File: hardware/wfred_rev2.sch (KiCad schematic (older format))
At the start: 8 parts, among them U101 L6920D

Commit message: Changed schematic to AA batteries and holder
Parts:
- removed B101: BATT_HOLDER, myFootprints:KEYSTONE1013, symbol BATT_HOLDER
- added B?: BATT_HOLDER_2, symbol BATT_HOLDER_2
- C101, C102, C104, C105: value 22u/25V -> 22u
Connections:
- wire segments 26 -> 25
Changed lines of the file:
@@
 P 2150 2900
 F 0 "C101" H 2150 3000 40  0000 L CNN
-F 1 "22u/25V" H 2156 2815 40  0000 L CNN
+F 1 "22u" H 2156 2815 40  0000 L CNN
 F 2 "Capacitors_SMD:C_0805_HandSoldering" H 2188 2750 30  0001 C CNN
 F 3 "" H 2150 2900 60  0000 C CNN
@@
 P 2450 2900
 F 0 "C102" H 2450 3000 40  0000 L CNN
-F 1 "22u/25V" H 2456 2815 40  0000 L CNN
+F 1 "22u" H 2456 2815 40  0000 L CNN
 F 2 "Capacitors_SMD:C_0805_HandSoldering" H 2488 2750 30  0001 C CNN
 F 3 "" H 2450 2900 60  0000 C CNN
@@
 P 6300 2600
 F 0 "C104" H 6300 2700 40  0000 L CNN
-F 1 "22u/25V" H 6306 2515 40  0000 L CNN
+F 1 "22u" H 6306 2515 40  0000 L CNN
 F 2 "Capacitors_SMD:C_0805_HandSoldering" H 6338 2450 30  0001 C CNN
 F 3 "" H 6300 2600 60  0000 C CNN
@@
 P 6600 2600
 F 0 "C105" H 6600 2700 40  0000 L CNN
-F 1 "22u/25V" H 6606 2515 40  0000 L CNN
+F 1 "22u" H 6606 2515 40  0000 L CNN
 F 2 "Capacitors_SMD:C_0805_HandSoldering" H 6638 2450 30  0001 C CNN
 F 3 "" H 6600 2600 60  0000 C CNN
@@
 $EndSheet
 Wire Wire Line
-	900  6100 1500 6100
-Wire Wire Line
 	900  3700 900  2600
 Wire Wire Line
 	1500 3700 1500 2800
 $Comp
-L BATT_HOLDER B101
-U 1 1 5A14A6C1
+L BATT_HOLDER_2 B?
+U 1 1 5BE48F43
 P 1200 4900
-F 0 "B101" H 1200 5000 60  0000 C CNN
-F 1 "BATT_HOLDER" H 1200 4900 60  0000 C CNN
-F 2 "myFootprints:KEYSTONE1013" H 1200 4900 60  0001 C CNN
+F 0 "B?" H 1200 5000 60  0000 C CNN
+F 1 "BATT_HOLDER_2" H 1200 4900 60  0000 C CNN
+F 2 "" H 1200 4900 60  0001 C CNN
 F 3 "" H 1200 4900 60  0001 C CNN
-F 4 "KEYSTONE 1013" H 1200 4900 60  0001 C CNN "Reichelt"
 	1    1200 4900
 	0    1    1    0

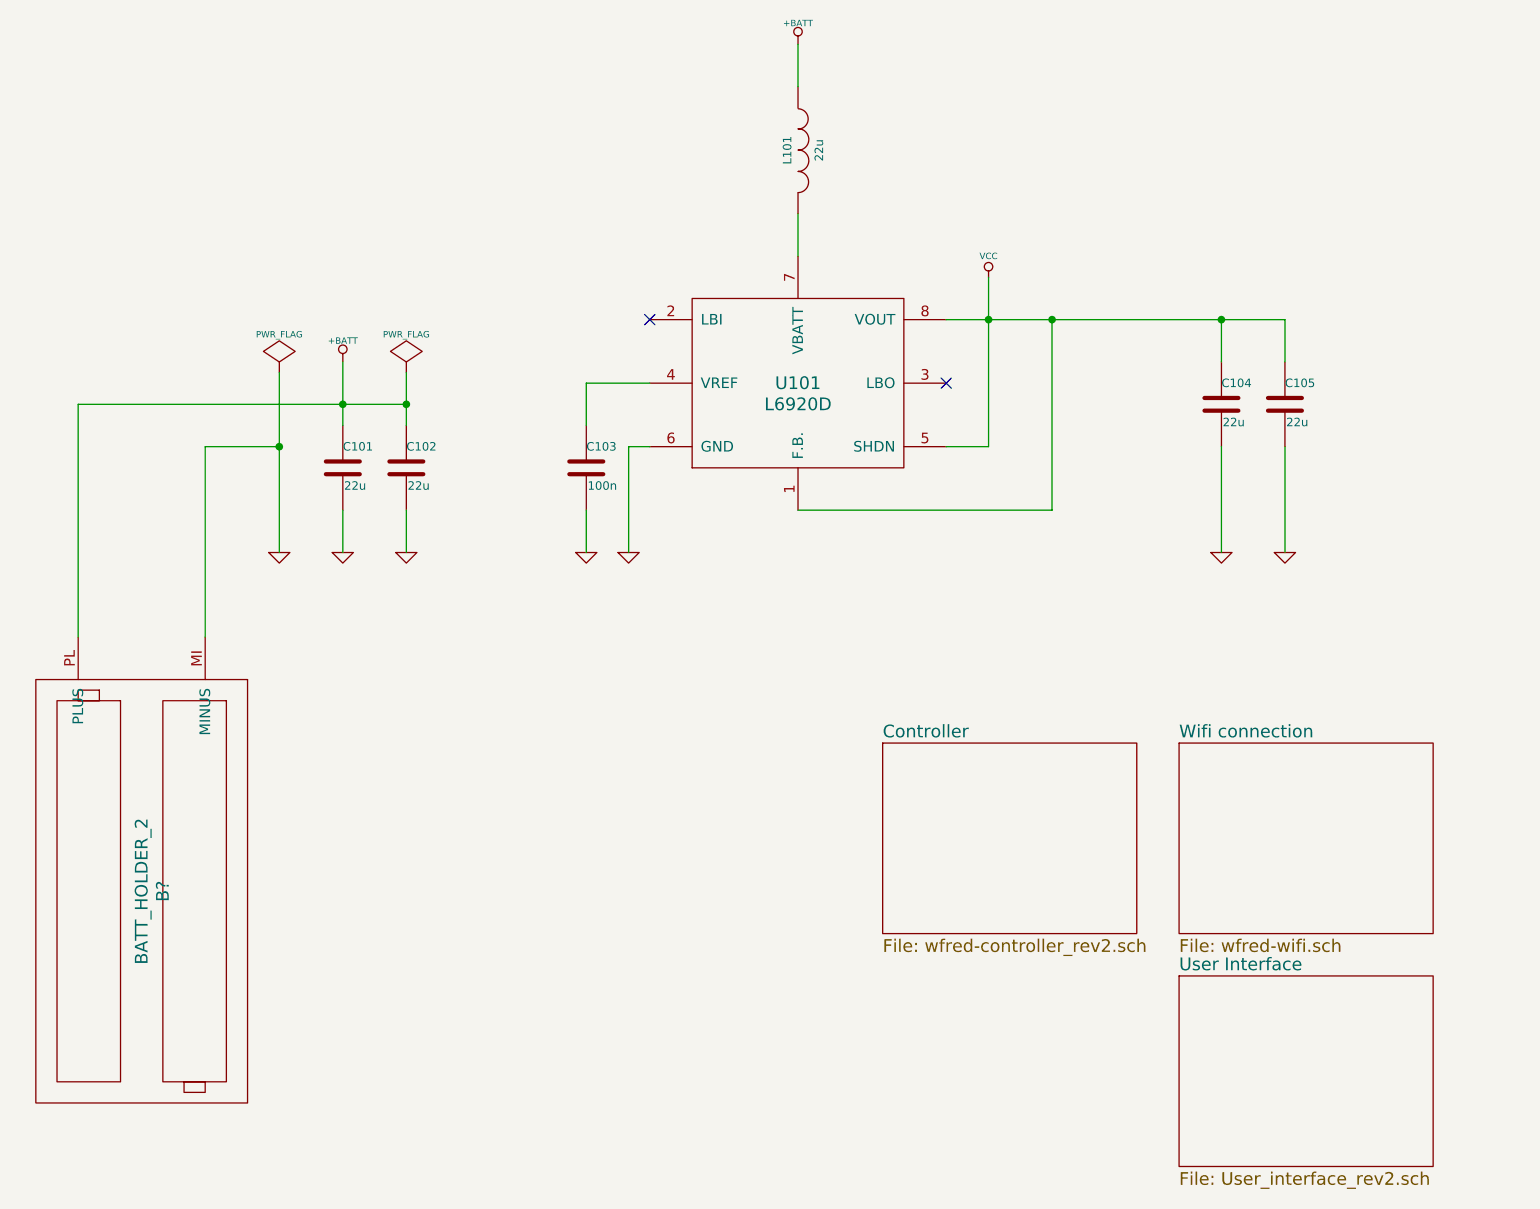
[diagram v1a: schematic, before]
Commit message: Small alignment fixes
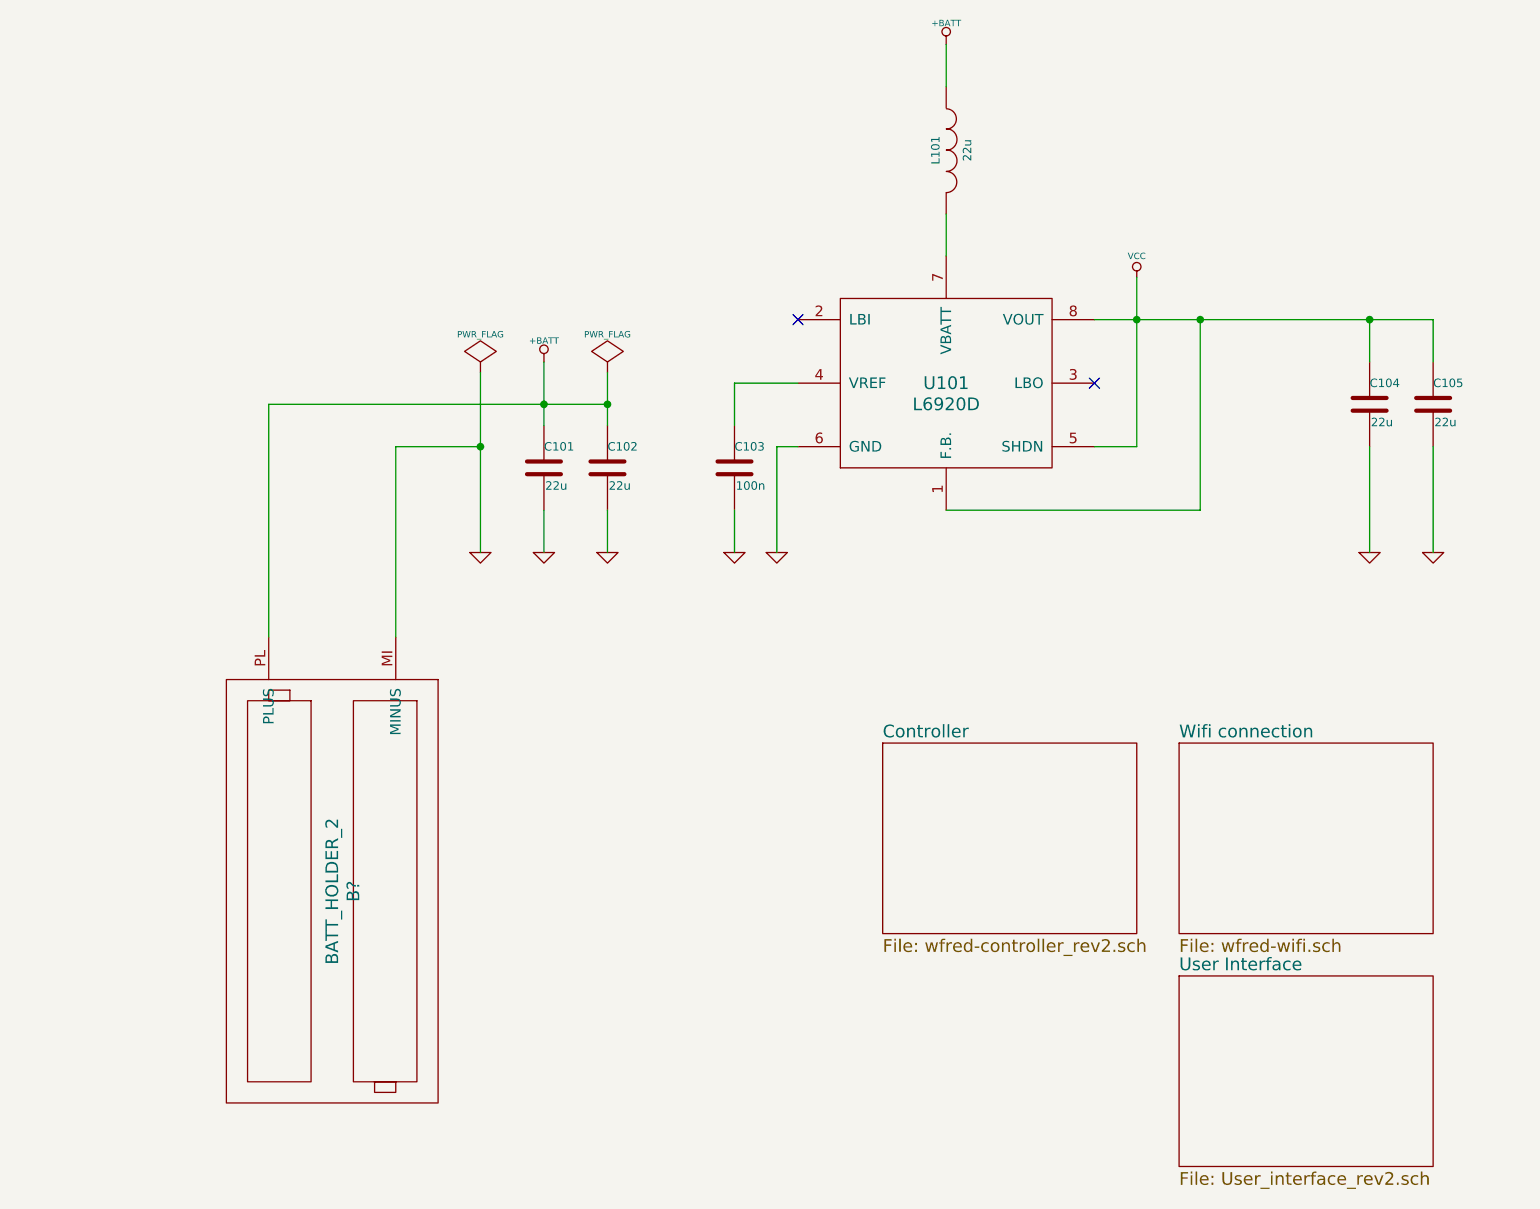
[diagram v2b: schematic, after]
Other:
- moved on the sheet: B?, C101, C102, C103, C104, C105, L101, U101

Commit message: Fixed ERC errors
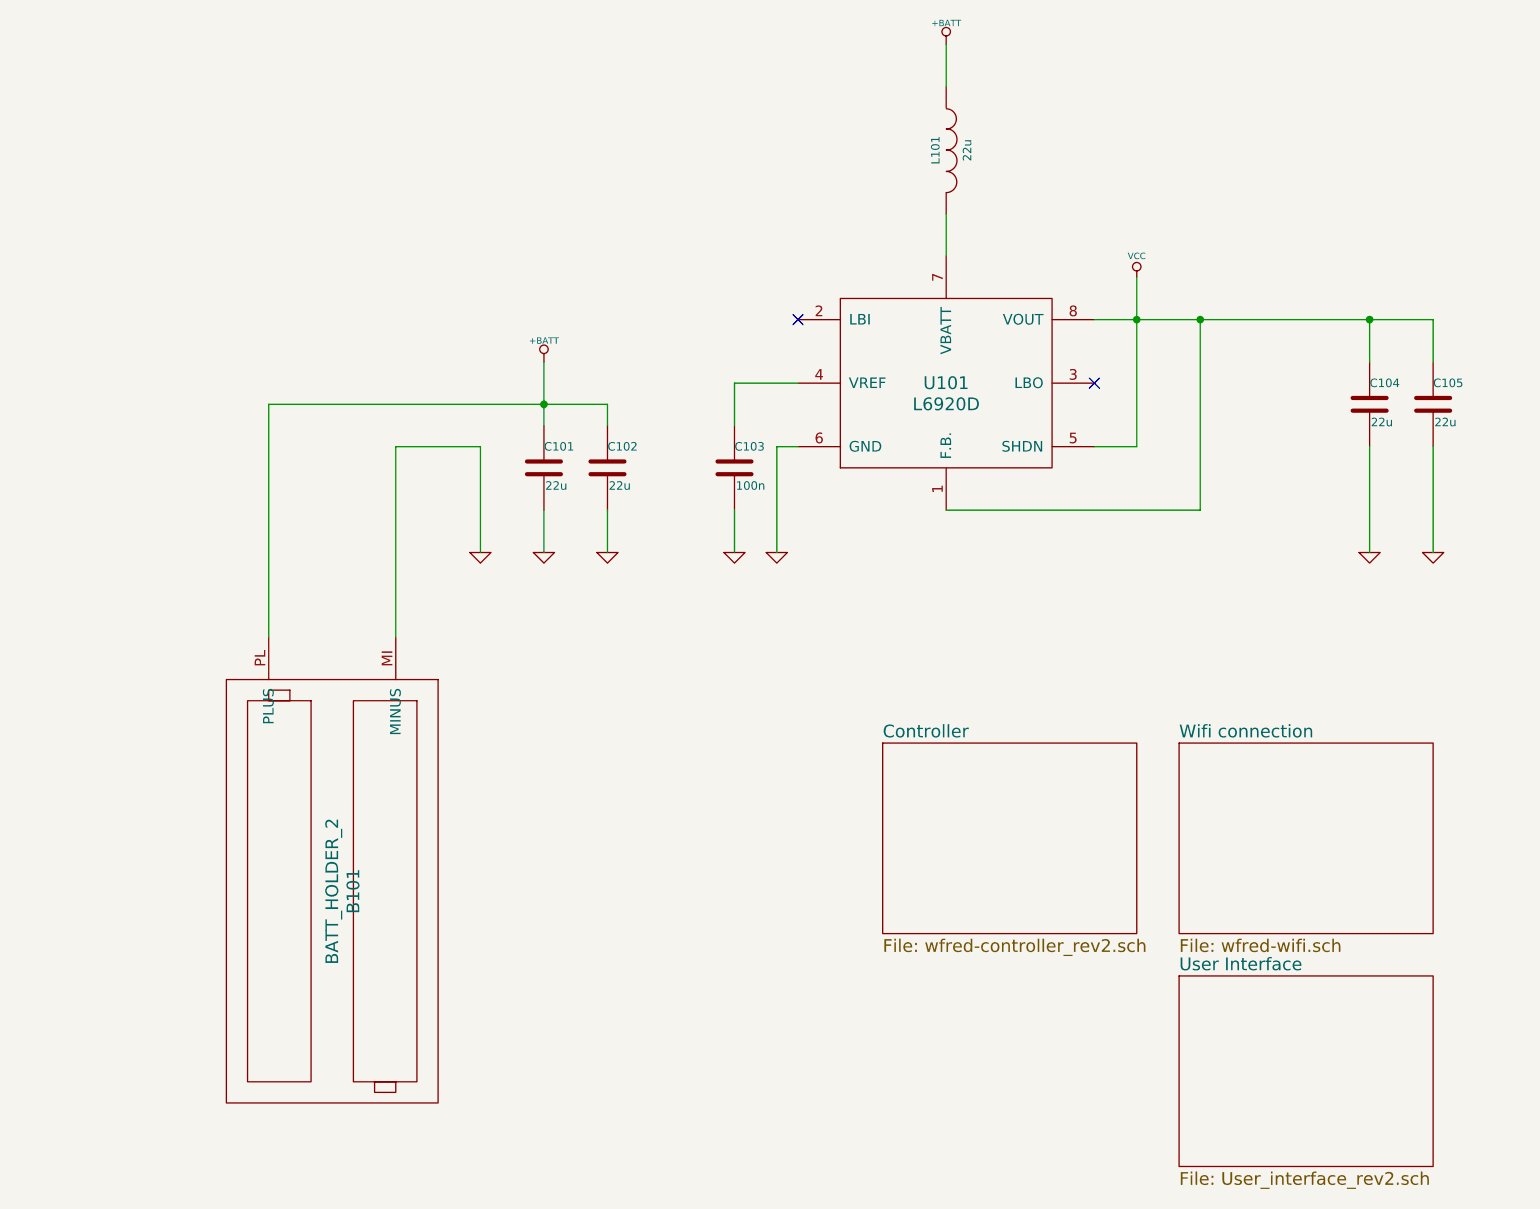
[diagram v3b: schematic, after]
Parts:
- gave numbers to parts that had none: 1
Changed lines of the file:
@@
 $EndDescr
 Wire Wire Line
-	3400 2450 3400 2600
-Wire Wire Line
-	3400 2600 3400 2700
-Wire Wire Line
-	1800 2600 3100 2600
-Wire Wire Line
-	3100 2600 3400 2600
-Wire Wire Line
-	3100 2400 3100 2600
-Wire Wire Line
-	3100 2600 3100 2700
+	1800 2600 3400 2600
+Wire Wire Line
+	3100 2400 3100 2700
 Connection ~ 3100 2600
 Wire Wire Line
 	2400 2800 2800 2800
 Wire Wire Line
-	2800 2450 2800 2800
-Wire Wire Line
-	2800 2800 2800 3300
-Wire Wire Line
 	3100 3100 3100 3300
 Wire Wire Line
@@
 	4000 3100 4000 3300
 Wire Wire Line
-	5900 2000 5900 2200
-Wire Wire Line
-	5900 2200 5900 2800
-Wire Wire Line
-	5700 2200 5900 2200
-Wire Wire Line
-	5900 2200 6200 2200
-Wire Wire Line
-	6200 2200 7000 2200
-Wire Wire Line
-	7000 2200 7300 2200
+	5900 2000 5900 2800
+Wire Wire Line
+	5700 2200 7300 2200
 Wire Wire Line
 	5900 2800 5700 2800
@@
 $EndComp
 $Comp
-L PWR_FLAG #FLG011
-U 1 1 59214833
-P 3400 2450
-F 0 "#FLG011" H 3400 2545 30  0001 C CNN
-F 1 "PWR_FLAG" H 3400 2630 30  0000 C CNN
-F 2 "" H 3400 2450 60  0001 C CNN
-F 3 "" H 3400 2450 60  0001 C CNN
-	1    3400 2450
-	1    0    0    -1
-$EndComp
-Connection ~ 3400 2600
-$Comp
-L PWR_FLAG #FLG012
-U 1 1 59214BB2
-P 2800 2450
-F 0 "#FLG012" H 2800 2545 30  0001 C CNN
-F 1 "PWR_FLAG" H 2800 2630 30  0000 C CNN
-F 2 "" H 2800 2450 60  0001 C CNN
-F 3 "" H 2800 2450 60  0001 C CNN
-	1    2800 2450
-	1    0    0    -1
-$EndComp
-Connection ~ 2800 2800
-$Comp
 L L6920D U101
 U 1 1 5920B393
@@
 	2400 3700 2400 2800
 $Comp
-L BATT_HOLDER_2 B?
+L BATT_HOLDER_2 B101
 U 1 1 5BE48F43
 P 2100 4900
-F 0 "B?" H 2100 5000 60  0000 C CNN
+F 0 "B101" H 2100 5000 60  0000 C CNN
 F 1 "BATT_HOLDER_2" H 2100 4900 60  0000 C CNN
 F 2 "" H 2100 4900 60  0001 C CNN
@@
 	0    1    1    0
 $EndComp
+Wire Wire Line
+	3400 2600 3400 2700
+Wire Wire Line
+	2800 2800 2800 3300
 $EndSCHEMATC

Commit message: Changed footprints for new enclosure:
- Speed potentiometer: P090S
- Direction switch: TMS1T4B5M2RE
- Loco selection switches: EG1249
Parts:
- B101: footprint (none) -> myFootprints:NEW_AGE_COMPACT_AA
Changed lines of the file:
@@
 F 0 "B101" H 2100 5000 60  0000 C CNN
 F 1 "BATT_HOLDER_2" H 2100 4900 60  0000 C CNN
-F 2 "" H 2100 4900 60  0001 C CNN
+F 2 "myFootprints:NEW_AGE_COMPACT_AA" H 2100 4900 60  0001 C CNN
 F 3 "" H 2100 4900 60  0001 C CNN
 	1    2100 4900
